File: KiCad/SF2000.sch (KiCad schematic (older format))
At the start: 36 parts, among them J1 Conn_2Rows-86Pins_even_odd, J2 Conn_01x02, U1 LM1117-3.3, U2 TPS73643DBV, U3 SN74CBT16211, U4 SN74CBT16211, U5 SN74CBT16211, U6 SN74AUP1T87DCKR

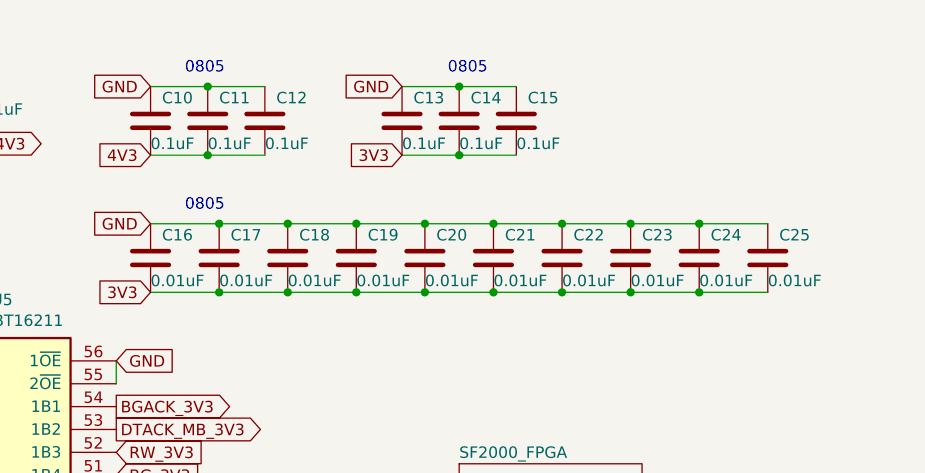
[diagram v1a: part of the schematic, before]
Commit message: added caps and did more routing
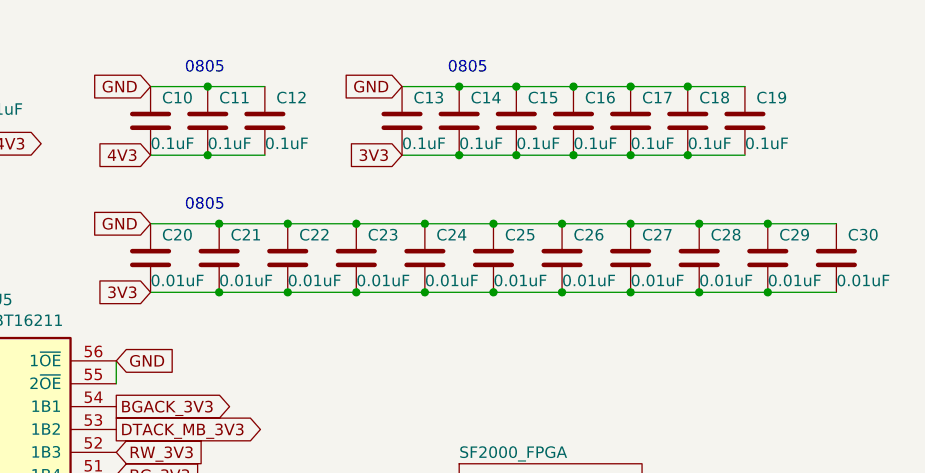
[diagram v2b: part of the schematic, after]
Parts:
- added C14, C15, C16, C17: 0.1uF, Capacitor_SMD:C_0805_2012Metric_Pad1.15x1.40mm_HandSolder, symbol Device:C
- added C30: 0.01uF, Capacitor_SMD:C_0805_2012Metric_Pad1.15x1.40mm_HandSolder, symbol Device:C
- renumbered C14 to C18, C15 to C19, C25 to C20, C16 to C21, C17 to C22, C18 to C23, C19 to C24, C20 to C25, C21 to C26, C22 to C27, C23 to C28, C24 to C29
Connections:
- net 3V3: now also C14.2, C15.2, C16.2, C17.2, C30.2
- net GND: now also C14.1, C15.1, C16.1, C17.1, C30.1
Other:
- moved on the sheet: C18, C19, C20, C21, C22, C23, C24, C25, C26, C27, C28, C29
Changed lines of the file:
@@
 	8300 1350 8600 1350
 $Comp
-L Device:C C17
+L Device:C C22
 U 1 1 623684C1
+P 8000 1500
+F 0 "C22" H 8050 1600 50  0000 L CNN
+F 1 "0.01uF" H 8000 1400 50  0000 L CNN
+F 2 "Capacitor_SMD:C_0805_2012Metric_Pad1.15x1.40mm_HandSolder" H 8038 1350 50  0001 C CNN
+F 3 "~" H 8000 1500 50  0001 C CNN
+	1    8000 1500
+	1    0    0    -1
+$EndComp
+$Comp
+L Device:C C26
+U 1 1 623684B7
+P 9200 1500
+F 0 "C26" H 9250 1600 50  0000 L CNN
+F 1 "0.01uF" H 9200 1400 50  0000 L CNN
+F 2 "Capacitor_SMD:C_0805_2012Metric_Pad1.15x1.40mm_HandSolder" H 9238 1350 50  0001 C CNN
+F 3 "~" H 9200 1500 50  0001 C CNN
+	1    9200 1500
+	1    0    0    -1
+$EndComp
+$Comp
+L Device:C C25
+U 1 1 623684AD
+P 8900 1500
+F 0 "C25" H 8950 1600 50  0000 L CNN
+F 1 "0.01uF" H 8900 1400 50  0000 L CNN
+F 2 "Capacitor_SMD:C_0805_2012Metric_Pad1.15x1.40mm_HandSolder" H 8938 1350 50  0001 C CNN
+F 3 "~" H 8900 1500 50  0001 C CNN
+	1    8900 1500
+	1    0    0    -1
+$EndComp
+$Comp
+L Device:C C21
+U 1 1 623684A3
 P 7700 1500
-F 0 "C17" H 7750 1600 50  0000 L CNN
+F 0 "C21" H 7750 1600 50  0000 L CNN
 F 1 "0.01uF" H 7700 1400 50  0000 L CNN
 F 2 "Capacitor_SMD:C_0805_2012Metric_Pad1.15x1.40mm_HandSolder" H 7738 1350 50  0001 C CNN
@@
 	1    0    0    -1
 $EndComp
-$Comp
-L Device:C C21
-U 1 1 623684B7
-P 8900 1500
-F 0 "C21" H 8950 1600 50  0000 L CNN
-F 1 "0.01uF" H 8900 1400 50  0000 L CNN
-F 2 "Capacitor_SMD:C_0805_2012Metric_Pad1.15x1.40mm_HandSolder" H 8938 1350 50  0001 C CNN
-F 3 "~" H 8900 1500 50  0001 C CNN
-	1    8900 1500
-	1    0    0    -1
-$EndComp
-$Comp
-L Device:C C20
-U 1 1 623684AD
+Wire Wire Line
+	8000 1650 8300 1650
+Connection ~ 8000 1650
+Wire Wire Line
+	7700 1650 8000 1650
+Connection ~ 7700 1650
+Wire Wire Line
+	7400 1650 7700 1650
+Wire Wire Line
+	8000 1350 8300 1350
+Connection ~ 8000 1350
+Wire Wire Line
+	7700 1350 8000 1350
+Connection ~ 7700 1350
+Wire Wire Line
+	7400 1350 7700 1350
+$Comp
+L Device:C C28
+U 1 1 6231D11D
+P 9800 1500
+F 0 "C28" H 9850 1600 50  0000 L CNN
+F 1 "0.01uF" H 9800 1400 50  0000 L CNN
+F 2 "Capacitor_SMD:C_0805_2012Metric_Pad1.15x1.40mm_HandSolder" H 9838 1350 50  0001 C CNN
+F 3 "~" H 9800 1500 50  0001 C CNN
+	1    9800 1500
+	1    0    0    -1
+$EndComp
+$Comp
+L Device:C C27
+U 1 1 6231C987
+P 9500 1500
+F 0 "C27" H 9550 1600 50  0000 L CNN
+F 1 "0.01uF" H 9500 1400 50  0000 L CNN
+F 2 "Capacitor_SMD:C_0805_2012Metric_Pad1.15x1.40mm_HandSolder" H 9538 1350 50  0001 C CNN
+F 3 "~" H 9500 1500 50  0001 C CNN
+	1    9500 1500
+	1    0    0    -1
+$EndComp
+$Comp
+L Device:C C24
+U 1 1 6231BC31
 P 8600 1500
-F 0 "C20" H 8650 1600 50  0000 L CNN
+F 0 "C24" H 8650 1600 50  0000 L CNN
 F 1 "0.01uF" H 8600 1400 50  0000 L CNN
 F 2 "Capacitor_SMD:C_0805_2012Metric_Pad1.15x1.40mm_HandSolder" H 8638 1350 50  0001 C CNN
@@
 	1    0    0    -1
 $EndComp
-$Comp
-L Device:C C16
-U 1 1 623684A3
+Text Notes 7550 1300 0    50   ~ 0
+0805
+$Comp
+L Device:C C23
+U 1 1 623192DF
+P 8300 1500
+F 0 "C23" H 8350 1600 50  0000 L CNN
+F 1 "0.01uF" H 8300 1400 50  0000 L CNN
+F 2 "Capacitor_SMD:C_0805_2012Metric_Pad1.15x1.40mm_HandSolder" H 8338 1350 50  0001 C CNN
+F 3 "~" H 8300 1500 50  0001 C CNN
+	1    8300 1500
+	1    0    0    -1
+$EndComp
+$Comp
+L Device:C C29
+U 1 1 623E0F2C
+P 10100 1500
+F 0 "C29" H 10150 1600 50  0000 L CNN
+F 1 "0.01uF" H 10100 1400 50  0000 L CNN
+F 2 "Capacitor_SMD:C_0805_2012Metric_Pad1.15x1.40mm_HandSolder" H 10138 1350 50  0001 C CNN
+F 3 "~" H 10100 1500 50  0001 C CNN
+	1    10100 1500
+	1    0    0    -1
+$EndComp
+$Comp
+L Device:C C20
+U 1 1 623E1D0B
 P 7400 1500
-F 0 "C16" H 7450 1600 50  0000 L CNN
+F 0 "C20" H 7450 1600 50  0000 L CNN
 F 1 "0.01uF" H 7400 1400 50  0000 L CNN
 F 2 "Capacitor_SMD:C_0805_2012Metric_Pad1.15x1.40mm_HandSolder" H 7438 1350 50  0001 C CNN
@@
 $EndComp
 Wire Wire Line
-	8000 1650 8300 1650
-Connection ~ 8000 1650
-Wire Wire Line
-	7700 1650 8000 1650
-Connection ~ 7700 1650
-Wire Wire Line
-	7400 1650 7700 1650
-Wire Wire Line
-	8000 1350 8300 1350
-Connection ~ 8000 1350
-Wire Wire Line
-	7700 1350 8000 1350
-Connection ~ 7700 1350
-Wire Wire Line
-	7400 1350 7700 1350
-$Comp
-L Device:C C23
-U 1 1 6231D11D
-P 9500 1500
-F 0 "C23" H 9550 1600 50  0000 L CNN
-F 1 "0.01uF" H 9500 1400 50  0000 L CNN
-F 2 "Capacitor_SMD:C_0805_2012Metric_Pad1.15x1.40mm_HandSolder" H 9538 1350 50  0001 C CNN
-F 3 "~" H 9500 1500 50  0001 C CNN
-	1    9500 1500
-	1    0    0    -1
-$EndComp
-$Comp
-L Device:C C22
-U 1 1 6231C987
-P 9200 1500
-F 0 "C22" H 9250 1600 50  0000 L CNN
-F 1 "0.01uF" H 9200 1400 50  0000 L CNN
-F 2 "Capacitor_SMD:C_0805_2012Metric_Pad1.15x1.40mm_HandSolder" H 9238 1350 50  0001 C CNN
-F 3 "~" H 9200 1500 50  0001 C CNN
-	1    9200 1500
-	1    0    0    -1
-$EndComp
-$Comp
-L Device:C C19
-U 1 1 6231BC31
-P 8300 1500
-F 0 "C19" H 8350 1600 50  0000 L CNN
-F 1 "0.01uF" H 8300 1400 50  0000 L CNN
-F 2 "Capacitor_SMD:C_0805_2012Metric_Pad1.15x1.40mm_HandSolder" H 8338 1350 50  0001 C CNN
-F 3 "~" H 8300 1500 50  0001 C CNN
-	1    8300 1500
-	1    0    0    -1
-$EndComp
-Text Notes 7550 1300 0    50   ~ 0
-0805
-$Comp
-L Device:C C18
-U 1 1 623192DF
-P 8000 1500
-F 0 "C18" H 8050 1600 50  0000 L CNN
-F 1 "0.01uF" H 8000 1400 50  0000 L CNN
-F 2 "Capacitor_SMD:C_0805_2012Metric_Pad1.15x1.40mm_HandSolder" H 8038 1350 50  0001 C CNN
-F 3 "~" H 8000 1500 50  0001 C CNN
-	1    8000 1500
-	1    0    0    -1
-$EndComp
-$Comp
-L Device:C C24
-U 1 1 623E0F2C
-P 9800 1500
-F 0 "C24" H 9850 1600 50  0000 L CNN
-F 1 "0.01uF" H 9800 1400 50  0000 L CNN
-F 2 "Capacitor_SMD:C_0805_2012Metric_Pad1.15x1.40mm_HandSolder" H 9838 1350 50  0001 C CNN
-F 3 "~" H 9800 1500 50  0001 C CNN
-	1    9800 1500
-	1    0    0    -1
-$EndComp
-$Comp
-L Device:C C25
-U 1 1 623E1D0B
-P 10100 1500
-F 0 "C25" H 10150 1600 50  0000 L CNN
-F 1 "0.01uF" H 10100 1400 50  0000 L CNN
-F 2 "Capacitor_SMD:C_0805_2012Metric_Pad1.15x1.40mm_HandSolder" H 10138 1350 50  0001 C CNN
-F 3 "~" H 10100 1500 50  0001 C CNN
-	1    10100 1500
-	1    0    0    -1
-$EndComp
-Wire Wire Line
 	9500 1350 9800 1350
 Connection ~ 9500 1350
@@
 	9800 1650 10100 1650
 $Comp
+L Device:C C18
+U 1 1 623F7CFB
+P 9750 900
+F 0 "C18" H 9800 1000 50  0000 L CNN
+F 1 "0.1uF" H 9750 800 50  0000 L CNN
+F 2 "Capacitor_SMD:C_0805_2012Metric_Pad1.15x1.40mm_HandSolder" H 9788 750 50  0001 C CNN
+F 3 "~" H 9750 900 50  0001 C CNN
+	1    9750 900
+	1    0    0    -1
+$EndComp
+$Comp
+L Device:C C19
+U 1 1 623F86B0
+P 10000 900
+F 0 "C19" H 10050 1000 50  0000 L CNN
+F 1 "0.1uF" H 10000 800 50  0000 L CNN
+F 2 "Capacitor_SMD:C_0805_2012Metric_Pad1.15x1.40mm_HandSolder" H 10038 750 50  0001 C CNN
+F 3 "~" H 10000 900 50  0001 C CNN
+	1    10000 900
+	1    0    0    -1
+$EndComp
+Wire Wire Line
+	8500 750  8750 750
+Connection ~ 8750 750
+Wire Wire Line
+	8750 750  9000 750
+Wire Wire Line
+	8500 1050 8750 1050
+Connection ~ 8750 1050
+Wire Wire Line
+	8750 1050 9000 1050
+$Comp
+L Device:C C16
+U 1 1 62441B62
+P 9250 900
+F 0 "C16" H 9300 1000 50  0000 L CNN
+F 1 "0.1uF" H 9250 800 50  0000 L CNN
+F 2 "Capacitor_SMD:C_0805_2012Metric_Pad1.15x1.40mm_HandSolder" H 9288 750 50  0001 C CNN
+F 3 "~" H 9250 900 50  0001 C CNN
+	1    9250 900
+	1    0    0    -1
+$EndComp
+Wire Wire Line
+	9000 750  9250 750
+Connection ~ 9000 750
+Wire Wire Line
+	9000 1050 9250 1050
+Connection ~ 9000 1050
+$Comp
+L Device:C C17
+U 1 1 62446240
+P 9500 900
+F 0 "C17" H 9550 1000 50  0000 L CNN
+F 1 "0.1uF" H 9500 800 50  0000 L CNN
+F 2 "Capacitor_SMD:C_0805_2012Metric_Pad1.15x1.40mm_HandSolder" H 9538 750 50  0001 C CNN
+F 3 "~" H 9500 900 50  0001 C CNN
+	1    9500 900
+	1    0    0    -1
+$EndComp
+$Comp
 L Device:C C14
-U 1 1 623F7CFB
+U 1 1 62446FAF
 P 8750 900
 F 0 "C14" H 8800 1000 50  0000 L CNN
@@
 $Comp
 L Device:C C15
-U 1 1 623F86B0
+U 1 1 62447982
 P 9000 900
 F 0 "C15" H 9050 1000 50  0000 L CNN
@@
 $EndComp
 Wire Wire Line
-	8500 750  8750 750
-Connection ~ 8750 750
-Wire Wire Line
-	8750 750  9000 750
-Wire Wire Line
-	8500 1050 8750 1050
-Connection ~ 8750 1050
-Wire Wire Line
-	8750 1050 9000 1050
+	9250 750  9500 750
+Connection ~ 9250 750
+Connection ~ 9500 750
+Wire Wire Line
+	9500 750  9750 750
+Connection ~ 9750 750
+Wire Wire Line
+	9750 750  10000 750
+Wire Wire Line
+	9250 1050 9500 1050
+Connection ~ 9250 1050
+Connection ~ 9500 1050
+Wire Wire Line
+	9500 1050 9750 1050
+Connection ~ 9750 1050
+Wire Wire Line
+	9750 1050 10000 1050
+$Comp
+L Device:C C30
+U 1 1 62485EA7
+P 10400 1500
+F 0 "C30" H 10450 1600 50  0000 L CNN
+F 1 "0.01uF" H 10400 1400 50  0000 L CNN
+F 2 "Capacitor_SMD:C_0805_2012Metric_Pad1.15x1.40mm_HandSolder" H 10438 1350 50  0001 C CNN
+F 3 "~" H 10400 1500 50  0001 C CNN
+	1    10400 1500
+	1    0    0    -1
+$EndComp
+Wire Wire Line
+	10100 1350 10400 1350
+Connection ~ 10100 1350
+Wire Wire Line
+	10100 1650 10400 1650
+Connection ~ 10100 1650
 $EndSCHEMATC

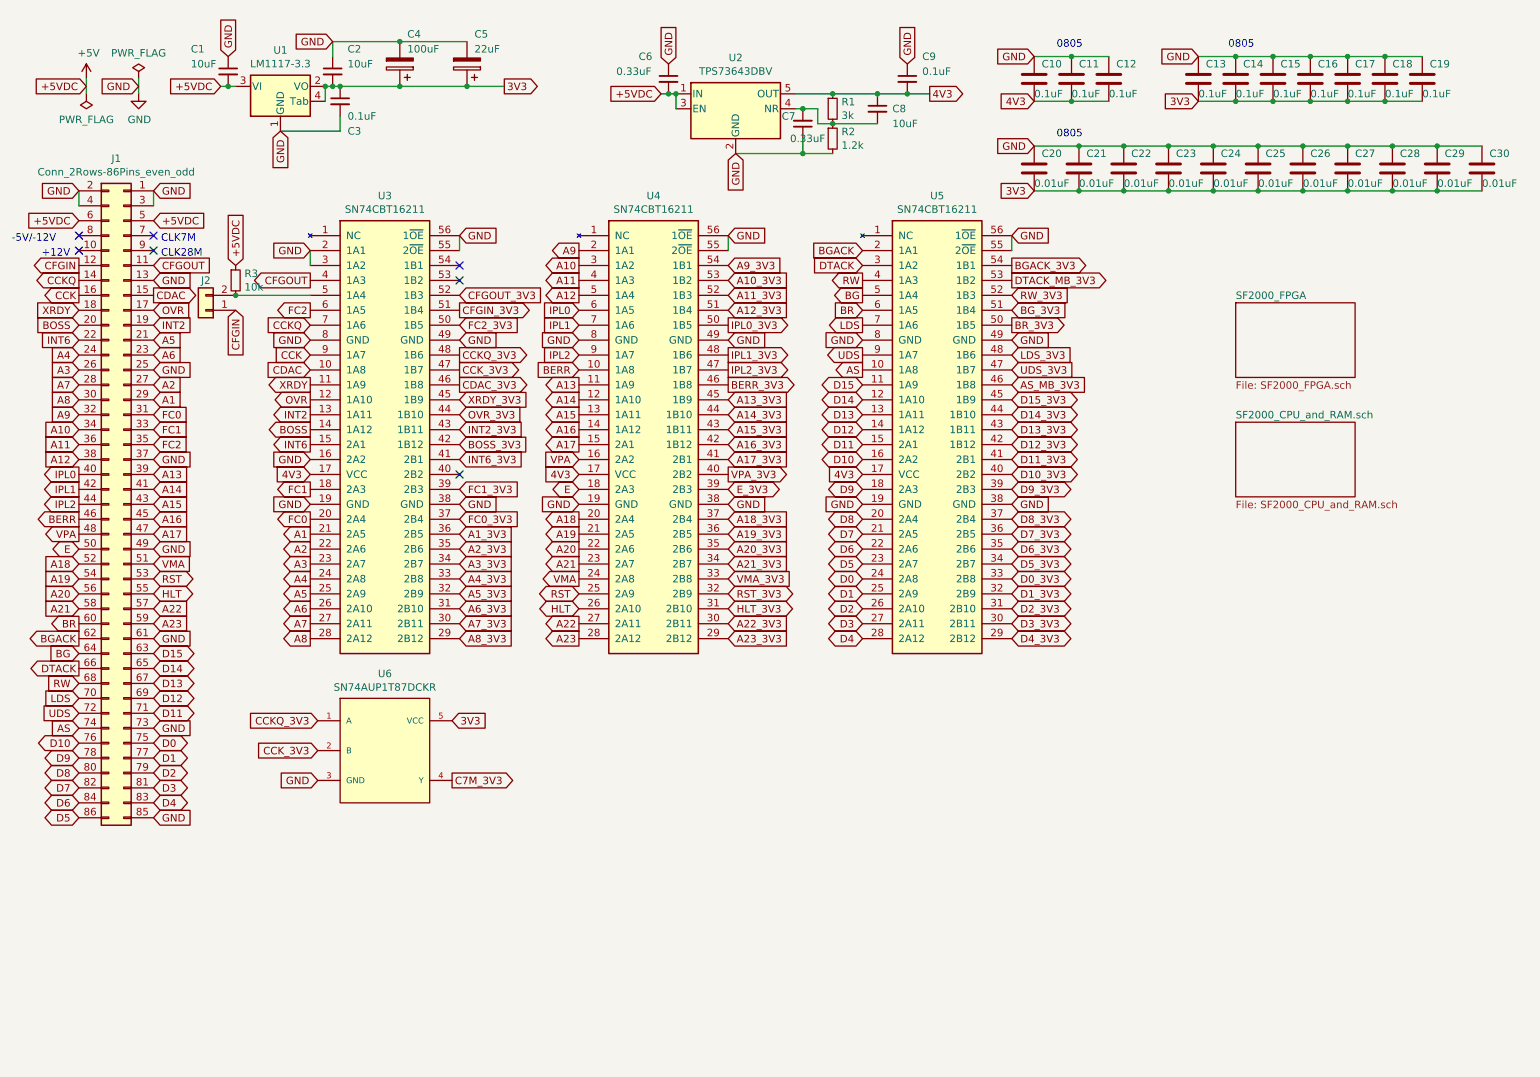
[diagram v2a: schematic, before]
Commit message: routing and caps fixes
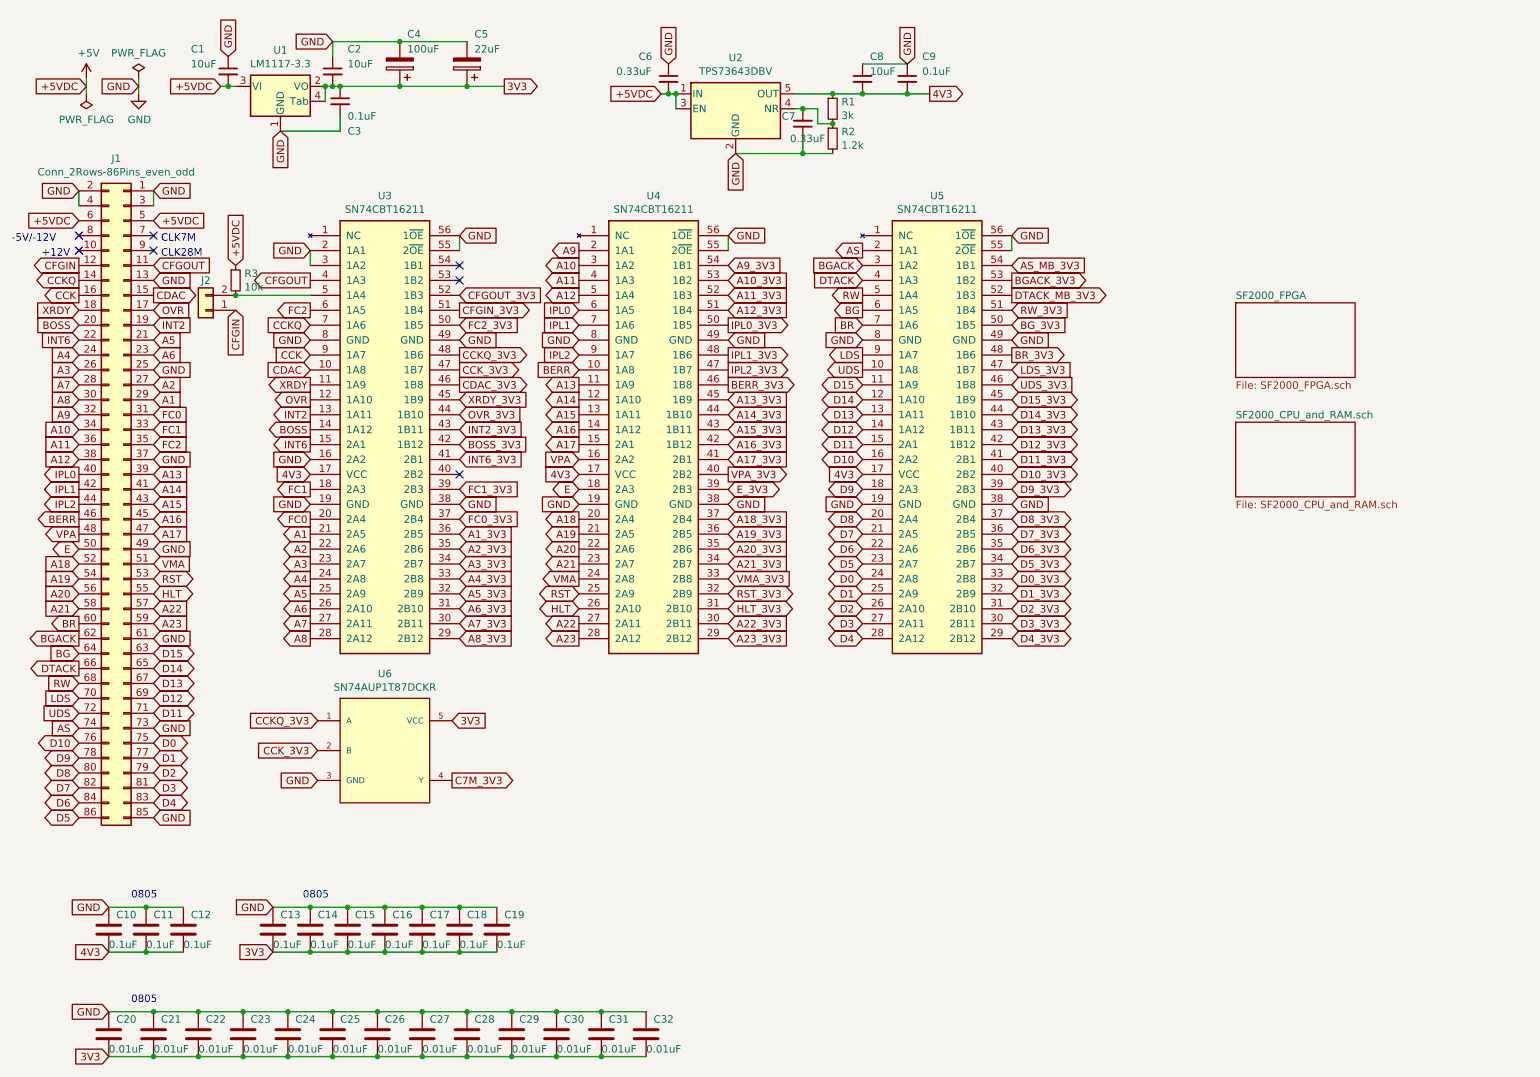
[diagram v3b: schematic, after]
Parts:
- added C31, C32: 0.01uF, Capacitor_SMD:C_0805_2012Metric_Pad1.15x1.40mm_HandSolder, symbol Device:C
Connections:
- net 3V3: now also C31.2, C32.2
- net 4V3: now also C8.2; no longer C8.1
- net AS: now also U5.2 (1A1); no longer U5.10 (1A8)
- net AS_MB_3V3: now also U5.54 (1B1); no longer U5.46 (1B8)
- net BG: now also U5.6 (1A5); no longer U5.5 (1A4)
- net BGACK: now also U5.3 (1A2); no longer U5.2 (1A1)
- net BGACK_3V3: now also U5.53 (1B2); no longer U5.54 (1B1)
- net BG_3V3: now also U5.50 (1B5); no longer U5.51 (1B4)
- net BR: now also U5.7 (1A6); no longer U5.6 (1A5)
- net BR_3V3: now also U5.48 (1B6); no longer U5.50 (1B5)
- net DTACK: now also U5.4 (1A3); no longer U5.3 (1A2)
- net DTACK_MB_3V3: now also U5.52 (1B3); no longer U5.53 (1B2)
- net GND: now also C8.1, C31.1, C32.1
- net LDS: now also U5.9 (1A7); no longer U5.7 (1A6)
- net LDS_3V3: now also U5.47 (1B7); no longer U5.48 (1B6)
- net RW: now also U5.5 (1A4); no longer U5.4 (1A3)
- net RW_3V3: now also U5.51 (1B4); no longer U5.52 (1B3)
- net UDS: now also U5.10 (1A8); no longer U5.9 (1A7)
- net UDS_3V3: now also U5.46 (1B8); no longer U5.47 (1B7)
- net at C7.2, R1.2, R2.1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: no longer C8.2
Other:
- moved on the sheet: C10, C11, C12, C13, C14, C15, C16, C17, C18, C19, C20, C21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

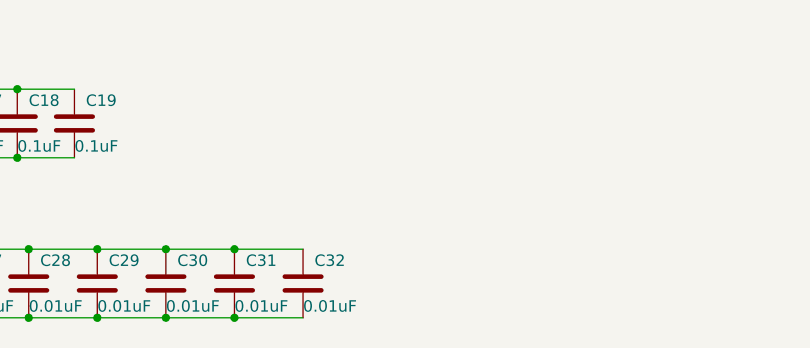
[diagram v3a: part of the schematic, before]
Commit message: more routing and caps fixes
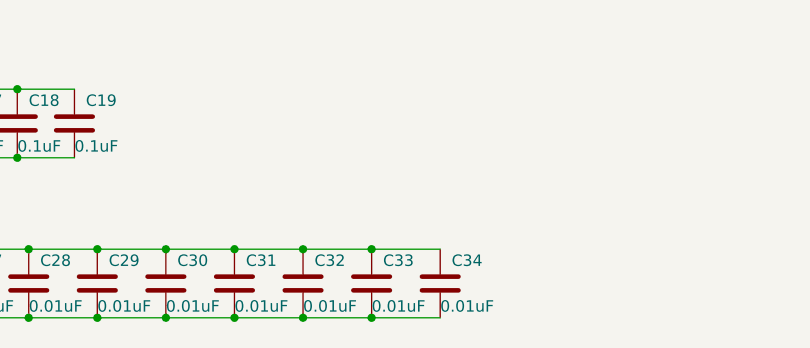
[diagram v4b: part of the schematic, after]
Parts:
- added C33, C34: 0.01uF, Capacitor_SMD:C_0805_2012Metric_Pad1.15x1.40mm_HandSolder, symbol Device:C
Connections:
- net 3V3: now also C33.2, C34.2
- net GND: now also C33.1, C34.1
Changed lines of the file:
@@
 	4500 7450 4800 7450
 Connection ~ 4500 7450
+$Comp
+L Device:C C33
+U 1 1 62559B16
+P 5100 7300
+F 0 "C33" H 5150 7400 50  0000 L CNN
+F 1 "0.01uF" H 5100 7200 50  0000 L CNN
+F 2 "Capacitor_SMD:C_0805_2012Metric_Pad1.15x1.40mm_HandSolder" H 5138 7150 50  0001 C CNN
+F 3 "~" H 5100 7300 50  0001 C CNN
+	1    5100 7300
+	1    0    0    -1
+$EndComp
+$Comp
+L Device:C C34
+U 1 1 6255AB6E
+P 5400 7300
+F 0 "C34" H 5450 7400 50  0000 L CNN
+F 1 "0.01uF" H 5400 7200 50  0000 L CNN
+F 2 "Capacitor_SMD:C_0805_2012Metric_Pad1.15x1.40mm_HandSolder" H 5438 7150 50  0001 C CNN
+F 3 "~" H 5400 7300 50  0001 C CNN
+	1    5400 7300
+	1    0    0    -1
+$EndComp
+Wire Wire Line
+	4800 7150 5100 7150
+Connection ~ 4800 7150
+Connection ~ 5100 7150
+Wire Wire Line
+	5100 7150 5400 7150
+Wire Wire Line
+	5400 7450 5100 7450
+Connection ~ 4800 7450
+Connection ~ 5100 7450
+Wire Wire Line
+	5100 7450 4800 7450
 $EndSCHEMATC
